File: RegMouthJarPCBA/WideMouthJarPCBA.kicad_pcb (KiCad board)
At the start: 2 copper layers, 48.3 x 48.3 mm, 33 parts, among them K1 CONN_3, P1 CONN_2, P3 CONN_2, P4 CONN_2, P5 CONN_2, P6 CONN_2, P7 CONN_2, U1 LTC2057, U2 LM399A, U3 LTC2057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

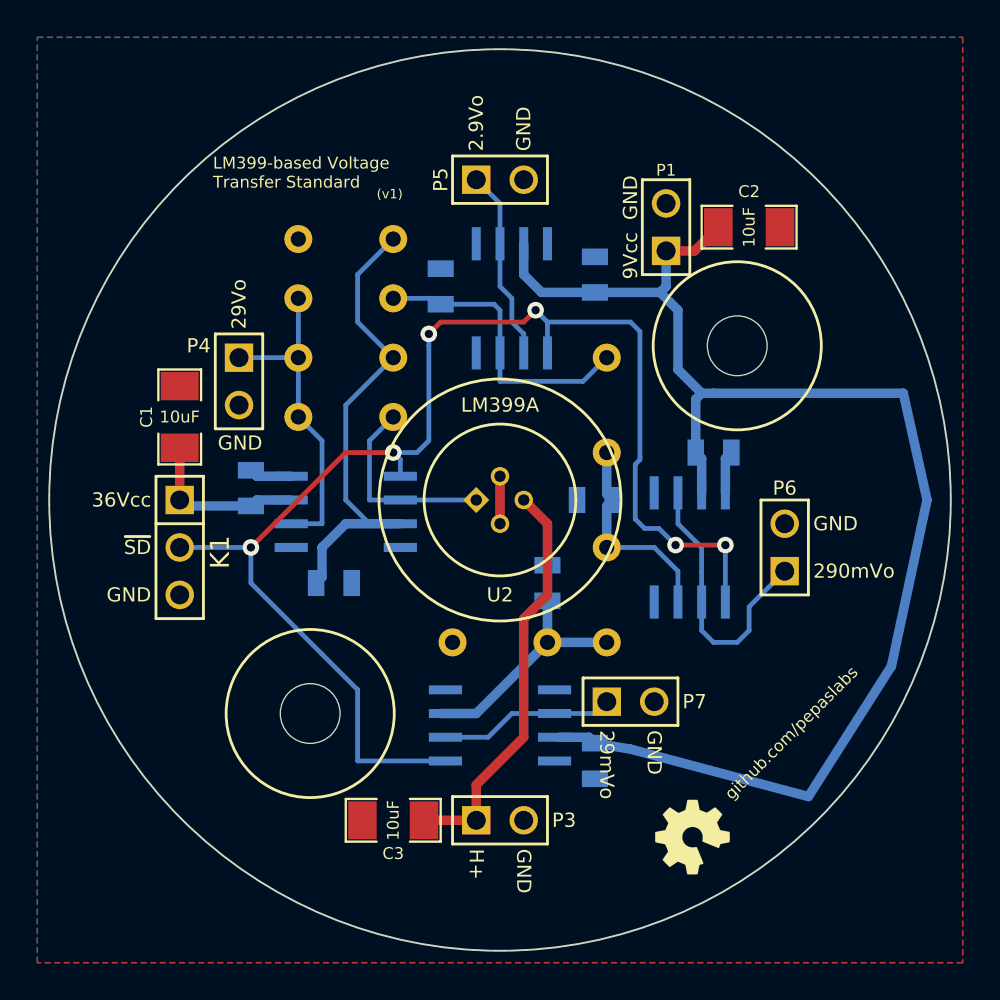
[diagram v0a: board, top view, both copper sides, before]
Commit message: implemented guard traces for LM399 reference board.  producing pcb's as v1.
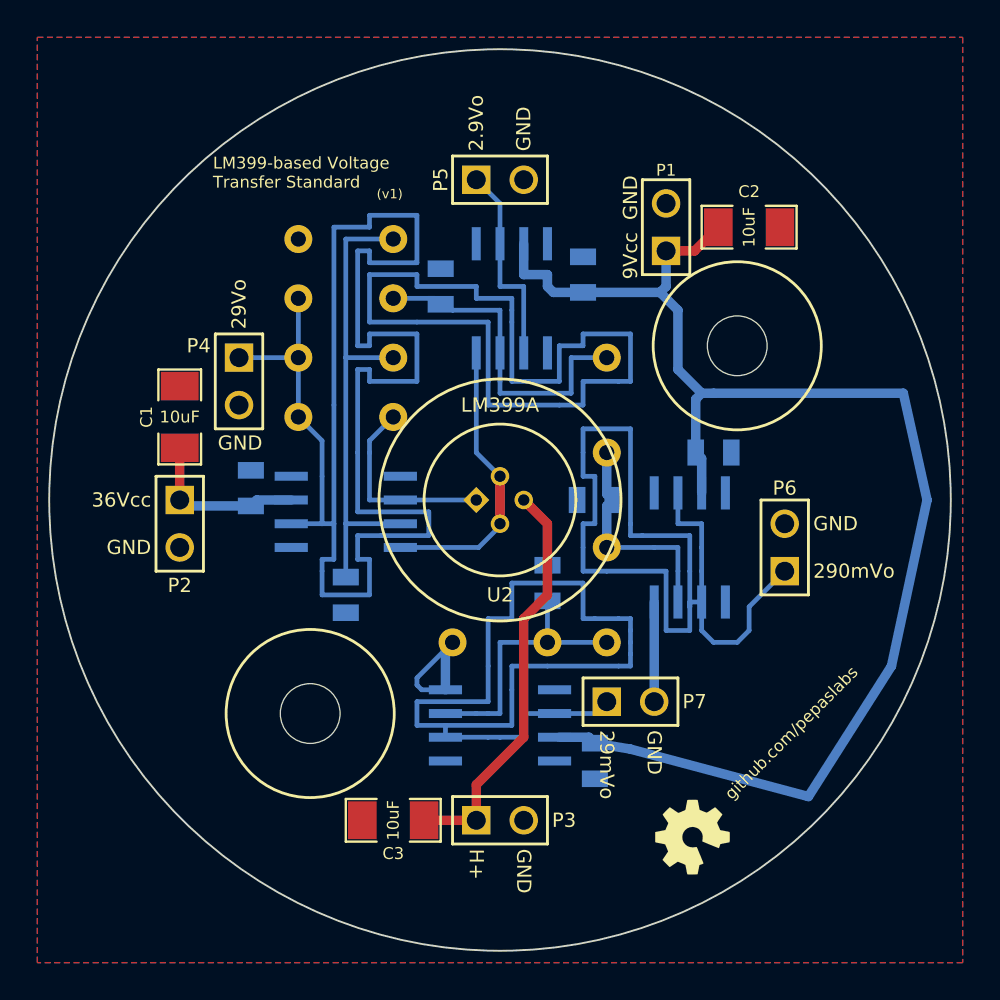
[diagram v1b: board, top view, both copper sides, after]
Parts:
- removed K1: CONN_3, PIN_ARRAY_3X1
- added P2: CONN_2, PIN_ARRAY_2X1, F.Cu at (190.5, 158.8)
- moved C5 0.90 mm to (199.4, 162.6), turned to 270 degrees
- moved C10 0.63 mm to (212.1, 145.4)
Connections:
- U1 pad 1: SD -> (no net)
- U1 pad 8: GND -> (no net)
- U3 pad 1: SD -> (no net)
- U3 pad 8: GND -> (no net)
- U4 pad 1: SD -> (no net)
- U4 pad 8: GND -> (no net)
- U5 pad 1: SD -> (no net)
- U5 pad 8: GND -> (no net)
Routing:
- net SD: track 73.9 -> 0.00 mm, vias 6 -> 0
- net 29Vo: track 17.4 -> 87.9 mm
- net (no net): track 0.00 -> 47.0 mm
- net 29mVo: track 9.93 -> 49.2 mm
- net 290mVo: track 14.9 -> 50.8 mm
- net GND: track 9.66 -> 30.9 mm
- net /29mV: track 12.7 -> 14.9 mm
- net /2.9V: track 16.7 -> 18.7 mm
- net 2.9Vo: track 10.3 -> 11.1 mm
- net /290mV: track 11.3 -> 12.1 mm
- net /Op-: track 26.8 -> 26.1 mm
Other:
- board text removed: "~SD"

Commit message: fixing a bug in the gaurd trace solder mask.
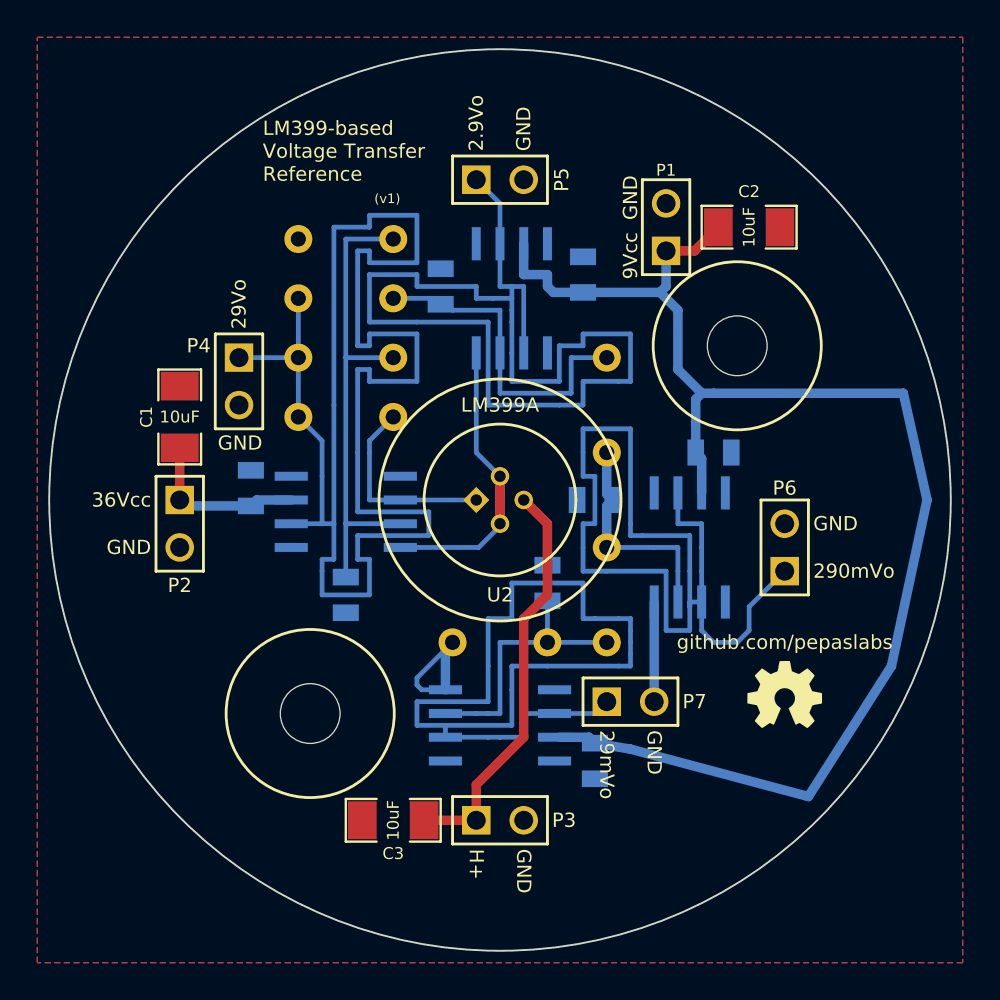
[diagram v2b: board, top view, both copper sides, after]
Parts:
- moved G*** 9.05 mm to (222.9, 167.9), turned to 0 degrees
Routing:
- net 2.9Vo: track 11.1 -> 58.7 mm
- net (no net): track 47.0 -> 0.00 mm
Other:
- board text added: "LM399-based Voltage Transfer Reference"
- board text removed: "LM399-based Voltage Transfer Standard"

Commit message: revising github url
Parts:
- moved G*** 0.13 mm to (222.9, 168.0)
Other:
- board text added: "github.com/pepaslabs/VoltStandard"
- board text removed: "github.com/pepaslabs"
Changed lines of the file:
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@@
   )
   (module OSHW-logo_silkscreen-front_4mm (layer F.Cu)
-    (at 222.885 167.894)
+    (at 222.885 168.021)
     (fp_text reference G*** (at 0 2.1209) (layer F.SilkS) hide
       (effects (font (size 0.18034 0.18034) (thickness 0.03556)))
@@
     (descr "Connecteurs 2 pins")
     (tags "CONN DEV")
-    (fp_text reference P2 (at 3.302 0 360) (layer F.SilkS)
+    (fp_text reference P2 (at -1.27 -2.286 360) (layer F.SilkS)
       (effects (font (size 0.762 0.762) (thickness 0.1524)))
     )
@@
     (effects (font (size 0.762 0.762) (thickness 0.1524)) (justify left))
   )
-  (gr_text "(v1)" (at 200.914 141.351) (layer F.SilkS)
+  (gr_text "(v1)" (at 210.185 147.955) (layer F.SilkS)
     (effects (font (size 0.508 0.508) (thickness 0.1016)) (justify left))
   )
-  (gr_text "LM399-based\nVoltage Transfer\nReference" (at 194.945 138.811) (layer F.SilkS)
-    (effects (font (size 0.762 0.762) (thickness 0.1524)) (justify left))
-  )
-  (gr_text github.com/pepaslabs (at 222.885 165.1) (layer F.SilkS)
-    (effects (font (size 0.762 0.762) (thickness 0.1524)))
+  (gr_text "LM399-based\nVoltage Transfer\nReference" (at 203.835 145.415) (layer F.SilkS)
+    (effects (font (size 0.762 0.762) (thickness 0.1524)) (justify left))
+  )
+  (gr_text github.com/pepaslabs/VoltStandard (at 194.564 163.449) (layer F.SilkS)
+    (effects (font (size 0.635 0.635) (thickness 0.127)))
   )
   (gr_circle (center 207.645 157.48) (end 187.325 157.48) (layer B.SilkS) (width 0.254))

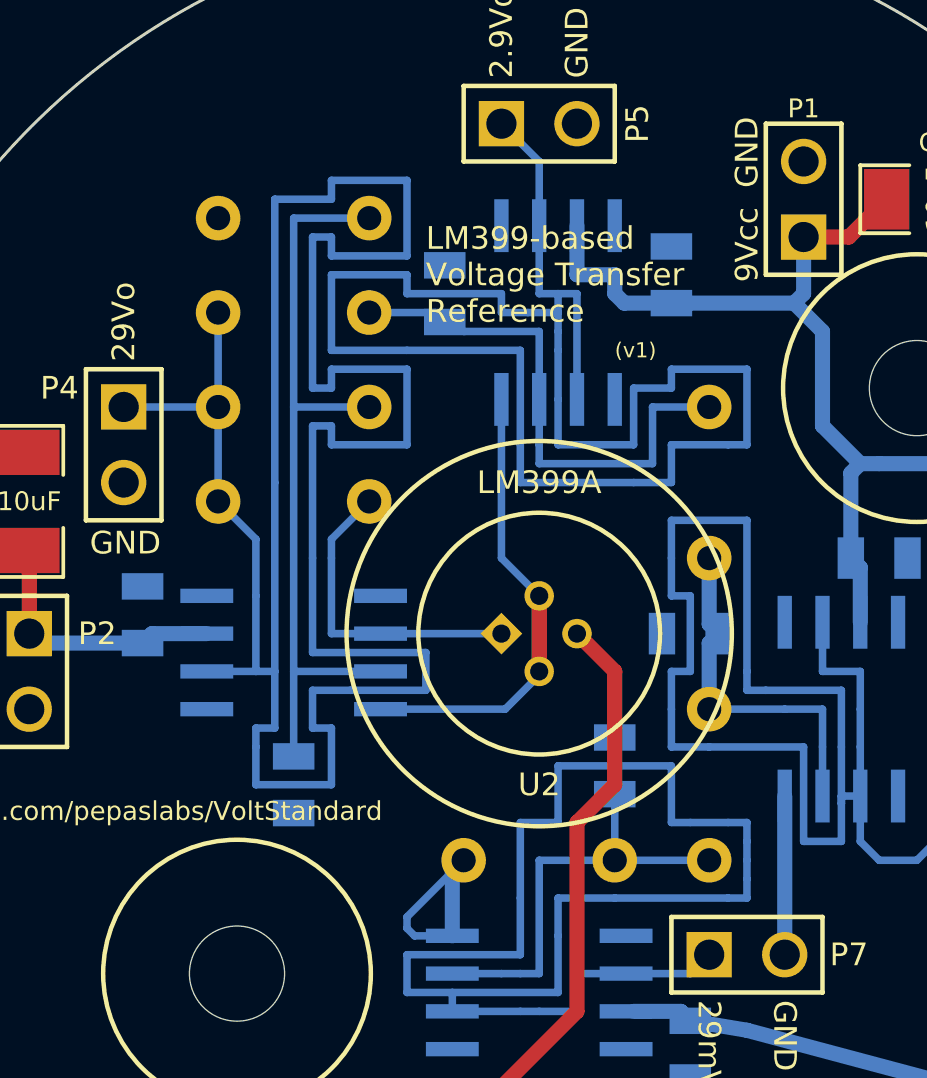
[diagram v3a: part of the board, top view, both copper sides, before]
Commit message: switching to combined 0.15" / 0.2" spaced resistor footprints.
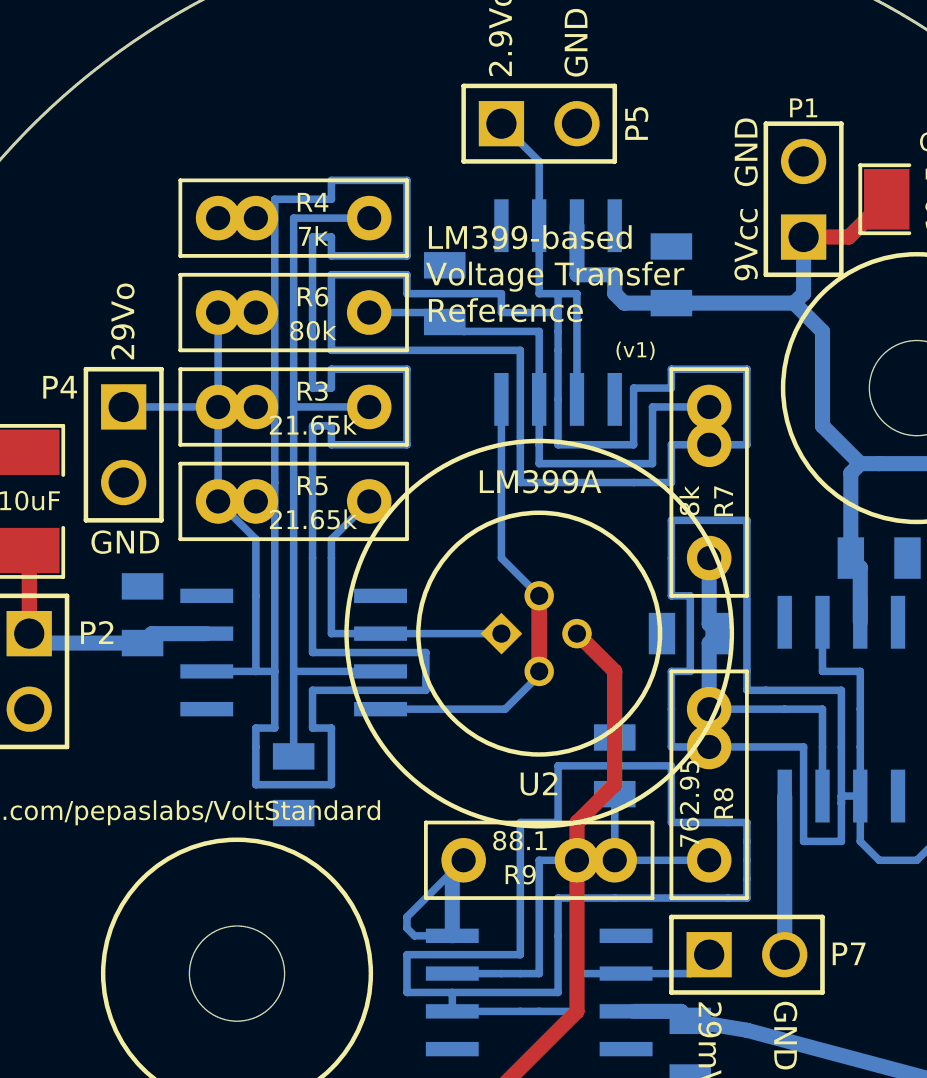
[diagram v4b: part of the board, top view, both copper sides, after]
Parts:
- R3, R4, R5, R6, R7, R8, R9: footprint R_BOX_02 -> R_BOX; moved to F.Cu
- moved R4 5.08 mm to (196.8, 143.5), turned to 0 degrees
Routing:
- net 2.9Vo: track 58.7 -> 11.7 mm
- net /2.9V: track 18.7 -> 65.7 mm
- net 290mVo: track 50.8 -> 16.3 mm
- net /290mV: track 12.1 -> 46.6 mm
- net GND: track 30.9 -> 33.4 mm
- net /Op-: track 26.1 -> 23.6 mm

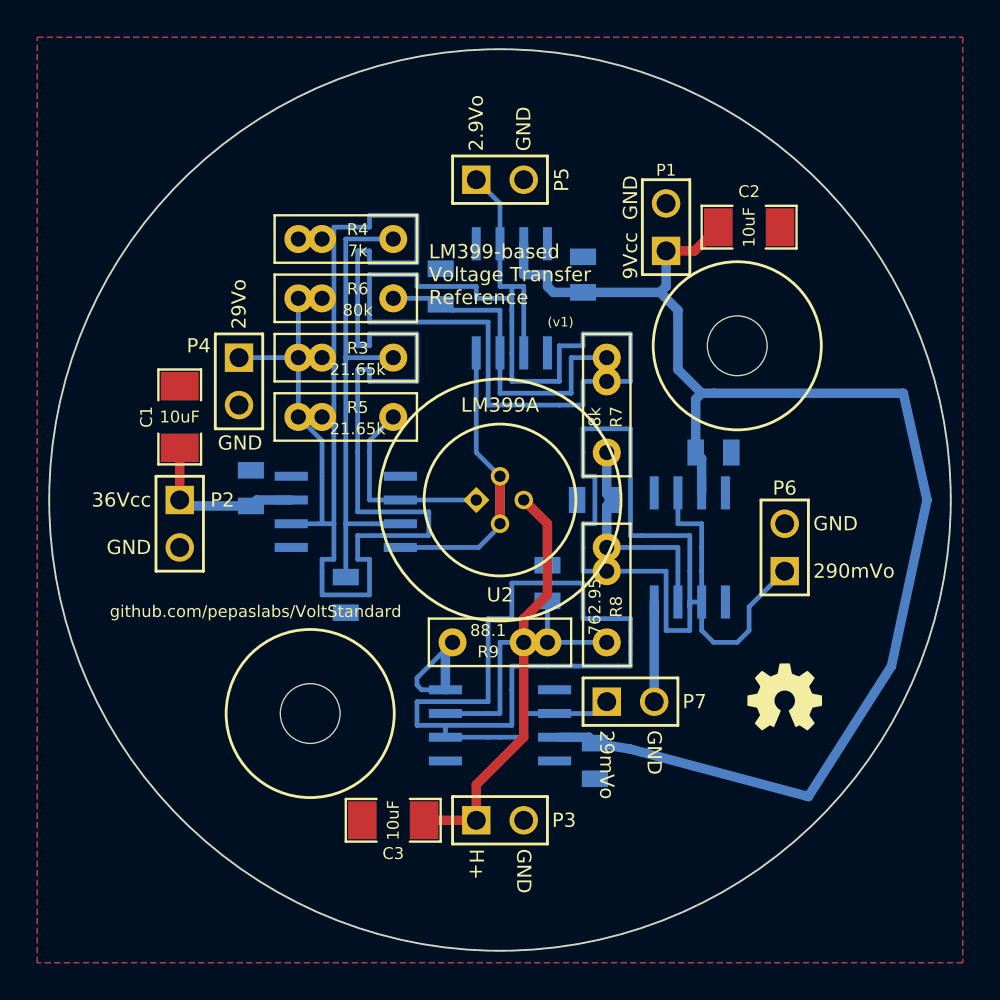
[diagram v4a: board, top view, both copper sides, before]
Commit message: substituting 10-pin LTC2057's.
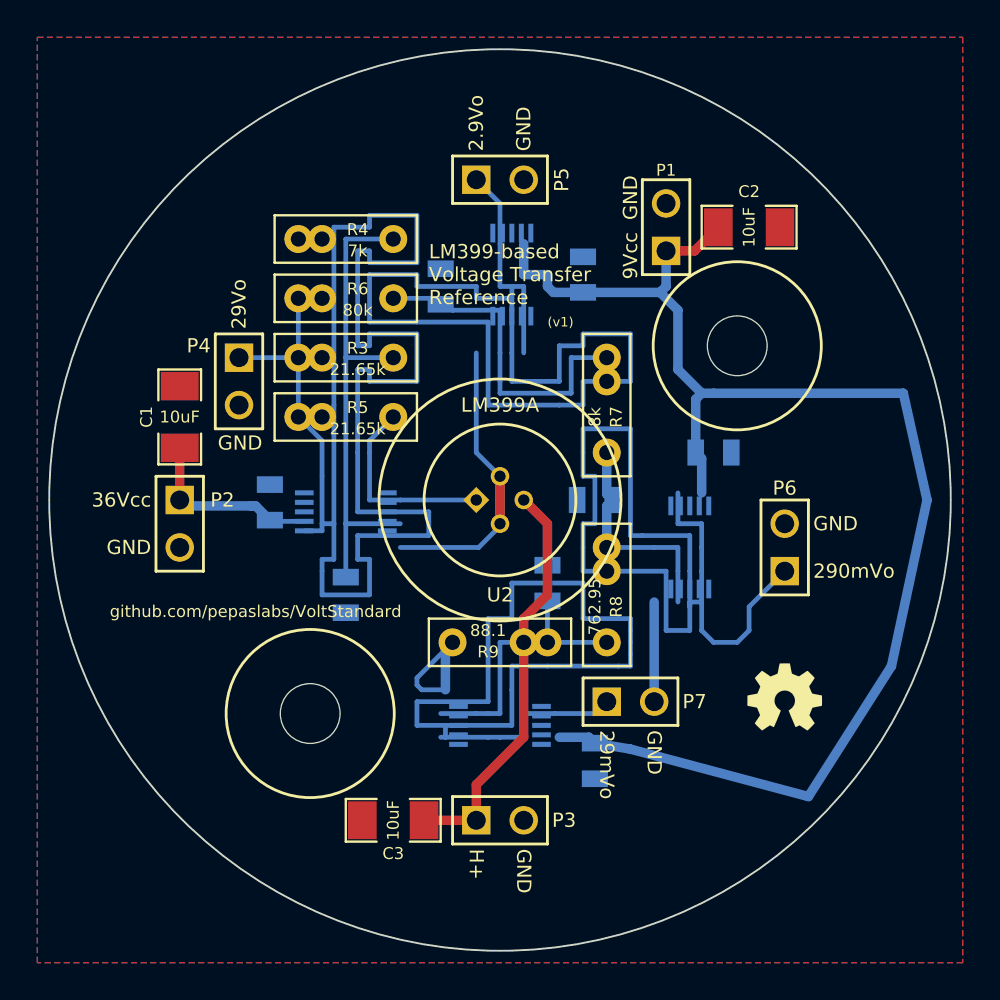
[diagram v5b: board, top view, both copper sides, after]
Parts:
- U1, U3, U4, U5: footprint SO-8 -> MSOP10-0.5
- moved U3 1.27 mm to (208.3, 145.4)
- moved C6 1.27 mm to (195.3, 157.6)
- turned U4 to 0 degrees
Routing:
- net 29mVo: track 49.2 -> 10.4 mm
- net (no net): track 0.00 -> 38.7 mm
- net /290mV: track 46.6 -> 60.2 mm
- net 290mVo: track 16.3 -> 2.69 mm
- net 2.9Vo: track 11.7 -> 1.80 mm
- net /2.9V: track 65.7 -> 71.1 mm
- net GND: track 33.4 -> 37.9 mm
- net 36V: track 9.03 -> 9.93 mm
